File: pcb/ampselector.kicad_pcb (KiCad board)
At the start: 2 copper layers, 85 x 100 mm, 24 parts, among them SW1 SW_Push, SW10 RotaryEncoder_Switch, SW2 SW_Push, SW3 SW_Push, SW4 SW_Push, SW5 SW_Push, SW6 SW_Push, SW7 SW_Push, SW8 SW_Push, SW9 RotaryEncoder_Switch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

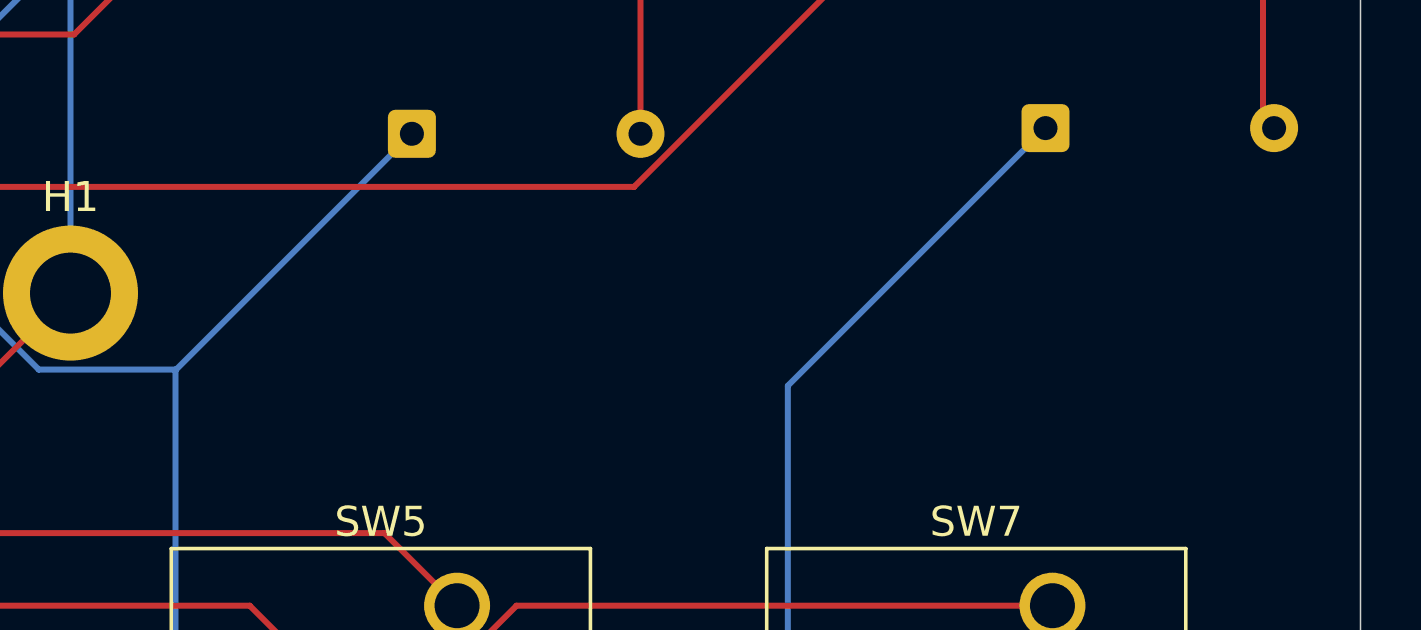
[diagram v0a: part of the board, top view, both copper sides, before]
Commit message: Added silkscreen
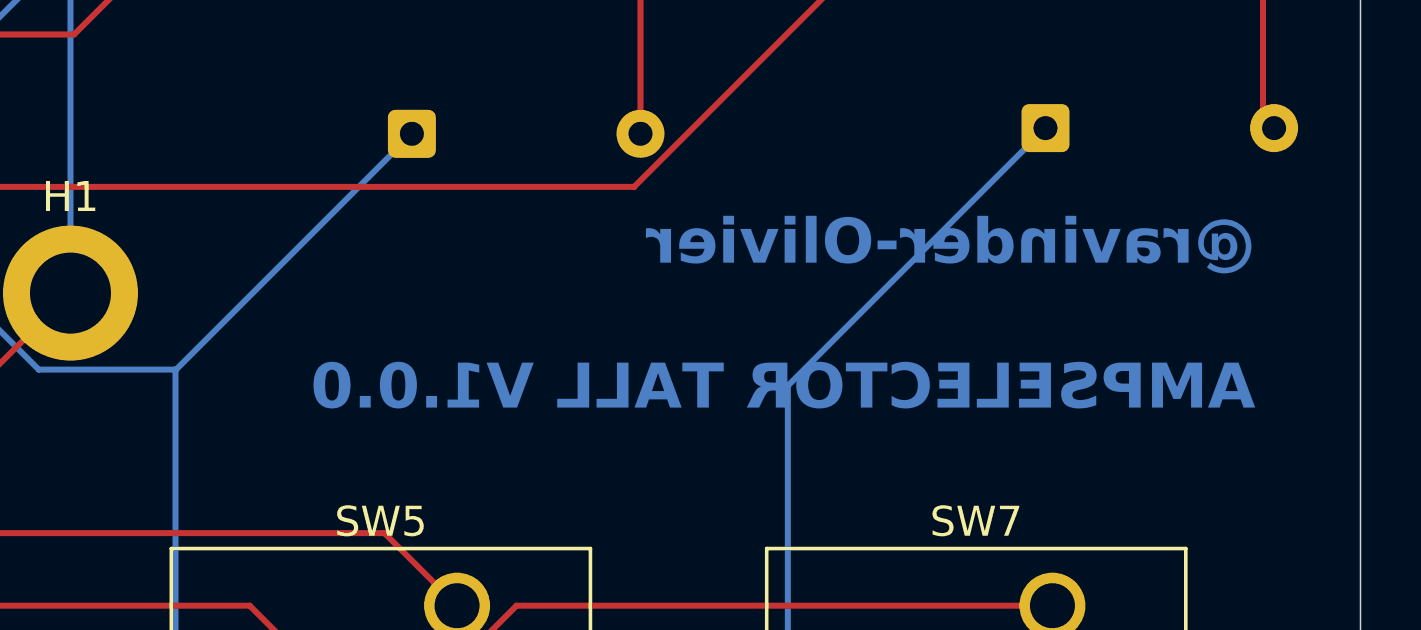
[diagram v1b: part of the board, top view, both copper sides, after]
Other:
- board text added: "@ravinder-Olivier AMPSELECTOR TALL V1.0.0"
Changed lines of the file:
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@@
 		(filling no)
 		(pcbplotparams
-			(layerselection 0x00000000_00000000_55555555_5755f5ff)
+			(layerselection 0x00000000_00000000_55555555_575555ff)
 			(plot_on_all_layers_selection 0x00000000_00000000_00000000_00000000)
 			(disableapertmacros no)
@@
 			(drillshape 0)
 			(scaleselection 1)
-			(outputdirectory "../../production/")
+			(outputdirectory "../Production/gerbers/")
 		)
 	)
@@
 		(layer "Edge.Cuts")
 	)
+	(gr_text "@ravinder-Olivier\n\nAMPSELECTOR TALL V1.0.0"
+		(at 127.5 90 -0)
+		(layer "B.Cu")
+		(effects
+			(font
+				(size 1.5 1.5)
+				(thickness 0.3)
+				(bold yes)
+			)
+			(justify left bottom mirror)
+		)
+	)
 	(segment

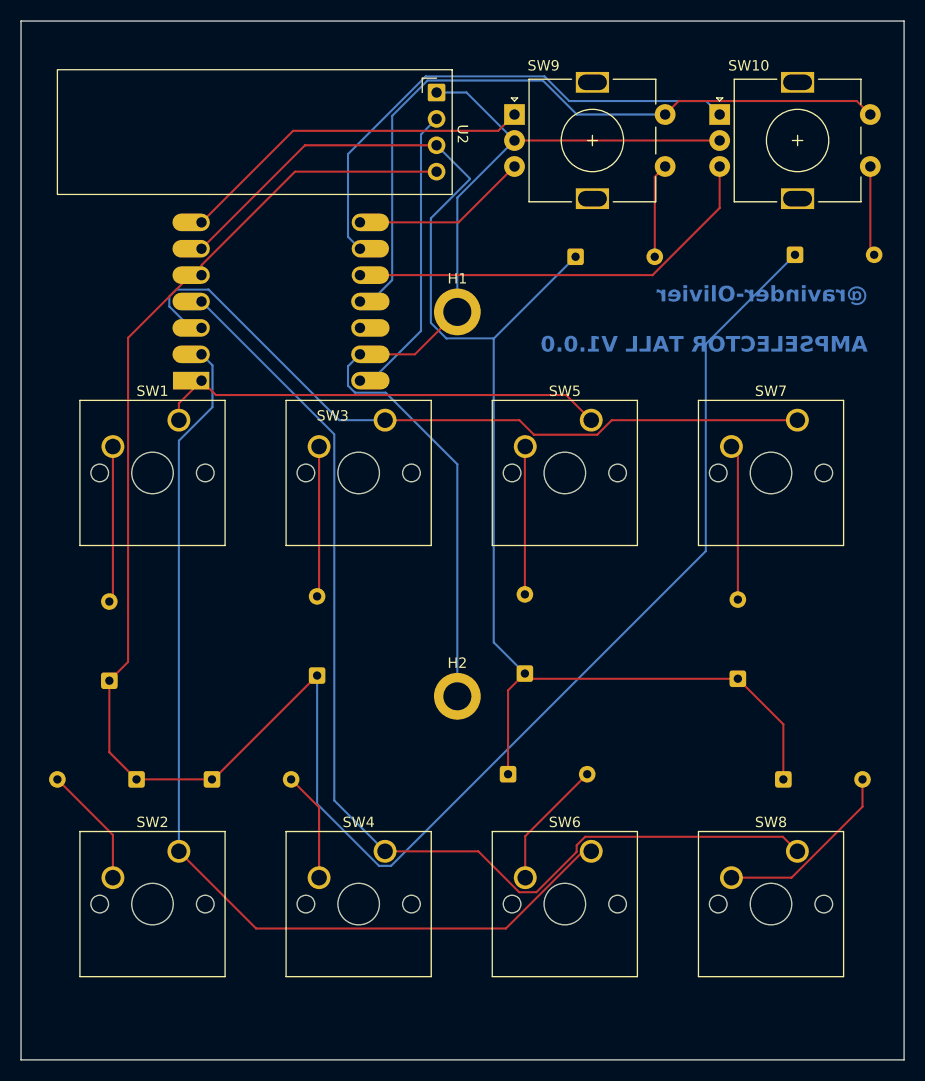
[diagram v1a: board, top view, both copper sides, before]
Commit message: changed text layer on silkscreen
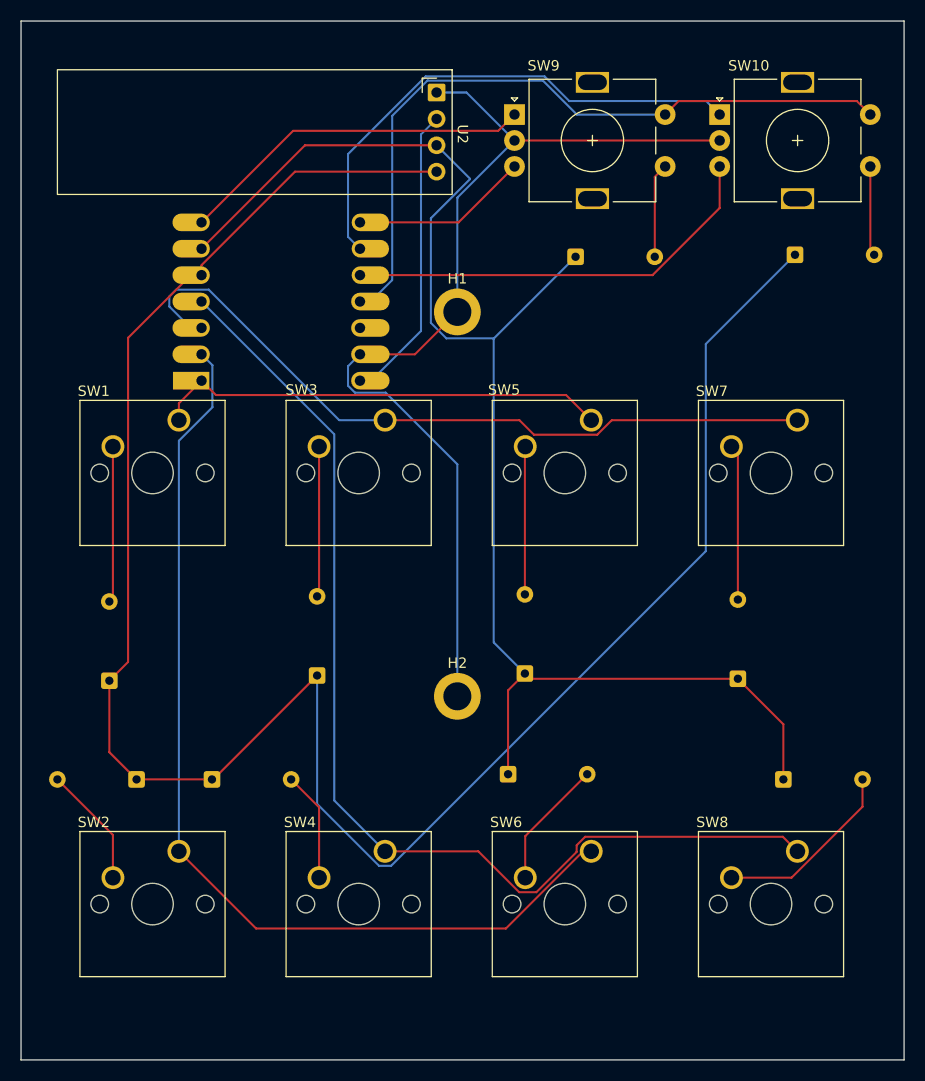
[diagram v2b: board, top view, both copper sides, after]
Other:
- board text added: "RAVINDER OLIVIER SINGH DADIALA @ravinder-Olivier v1.0.0 AMPSELECTOR"
- board text removed: "@ravinder-Olivier AMPSELECTOR TALL V1.0.0"
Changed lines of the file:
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@@
 		(tags "Cherry MX keyswitch 1.00u PCB")
 		(property "Reference" "SW6"
-			(at -2.54 -2.794 0)
+			(at -8.194286 -2.794 0)
 			(layer "F.SilkS")
 			(effects
@@
 		)
 		(fp_text user "${REFERENCE}"
-			(at -2.54 -2.794 0)
+			(at -8.194286 -2.794 0)
 			(layer "F.Fab")
 			(effects
@@
 		(tags "Cherry MX keyswitch 1.00u PCB")
 		(property "Reference" "SW1"
-			(at -2.54 -2.794 0)
+			(at -8.194286 -2.794 0)
 			(layer "F.SilkS")
 			(effects
@@
 		)
 		(fp_text user "${REFERENCE}"
-			(at -2.54 -2.794 0)
+			(at -8.194286 -2.794 0)
 			(layer "F.Fab")
 			(effects
@@
 		(tags "Cherry MX keyswitch 1.00u PCB")
 		(property "Reference" "SW5"
-			(at -2.54 -2.794 0)
+			(at -8.385715 -2.92 0)
 			(layer "F.SilkS")
 			(effects
@@
 		)
 		(fp_text user "${REFERENCE}"
-			(at -2.54 -2.794 0)
+			(at -8.385715 -2.92 0)
 			(layer "F.Fab")
 			(effects
@@
 		(tags "Cherry MX keyswitch 1.00u PCB")
 		(property "Reference" "SW7"
-			(at -2.54 -2.794 0)
+			(at -8.231429 -2.794 0)
 			(layer "F.SilkS")
 			(effects
@@
 		)
 		(fp_text user "${REFERENCE}"
-			(at -2.54 -2.794 0)
+			(at -8.231429 -2.794 0)
 			(layer "F.Fab")
 			(effects
@@
 		(tags "Cherry MX keyswitch 1.00u PCB")
 		(property "Reference" "SW4"
-			(at -2.54 -2.794 0)
+			(at -8.194286 -2.794 0)
 			(layer "F.SilkS")
 			(effects
@@
 		)
 		(fp_text user "${REFERENCE}"
-			(at -2.54 -2.794 0)
+			(at -8.194286 -2.794 0)
 			(layer "F.Fab")
 			(effects
@@
 		(tags "Cherry MX keyswitch 1.00u PCB")
 		(property "Reference" "SW3"
-			(at -5.04 -0.42 0)
+			(at -8.04 -2.92 0)
 			(layer "F.SilkS")
 			(effects
@@
 		)
 		(fp_text user "${REFERENCE}"
-			(at -5.04 -0.42 0)
+			(at -8.04 -2.92 0)
 			(layer "F.Fab")
 			(effects
@@
 		(tags "Cherry MX keyswitch 1.00u PCB")
 		(property "Reference" "SW8"
-			(at -2.54 -2.794 0)
+			(at -8.194286 -2.794 0)
 			(layer "F.SilkS")
 			(effects
@@
 		)
 		(property "Value" "SW_Push"
-			(at 4.935 -44.071 0)
+			(at -2.231429 12.954 0)
 			(layer "F.Fab")
 			(effects
@@
 		)
 		(fp_text user "${REFERENCE}"
-			(at -2.54 -2.794 0)
+			(at -8.194286 -2.794 0)
 			(layer "F.Fab")
 			(effects
@@
 		(tags "Cherry MX keyswitch 1.00u PCB")
 		(property "Reference" "SW2"
-			(at -2.54 -2.794 0)
+			(at -8.194286 -2.794 0)
 			(layer "F.SilkS")
 			(effects
@@
 		)
 		(fp_text user "${REFERENCE}"
-			(at -2.54 -2.794 0)
+			(at -8.194286 -2.794 0)
 			(layer "F.Fab")
 			(effects
@@
 		(layer "Edge.Cuts")
 	)
-	(gr_text "@ravinder-Olivier\n\nAMPSELECTOR TALL V1.0.0"
-		(at 127.5 90 -0)
-		(layer "B.Cu")
+	(gr_text "RAVINDER OLIVIER SINGH DADIALA\n@ravinder-Olivier\nv1.0.0\n\nAMPSELECTOR"
+		(at 76.5 70.5 0)
+		(layer "B.SilkS")
 		(effects
 			(font
-				(size 1.5 1.5)
-				(thickness 0.3)
+				(size 1 1)
+				(thickness 0.2)
 				(bold yes)
+				(italic yes)
 			)
 			(justify left bottom mirror)
